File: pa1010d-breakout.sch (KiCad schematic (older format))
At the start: 2 parts, among them J1 Conn_01x08_Male, U1 PA1010D

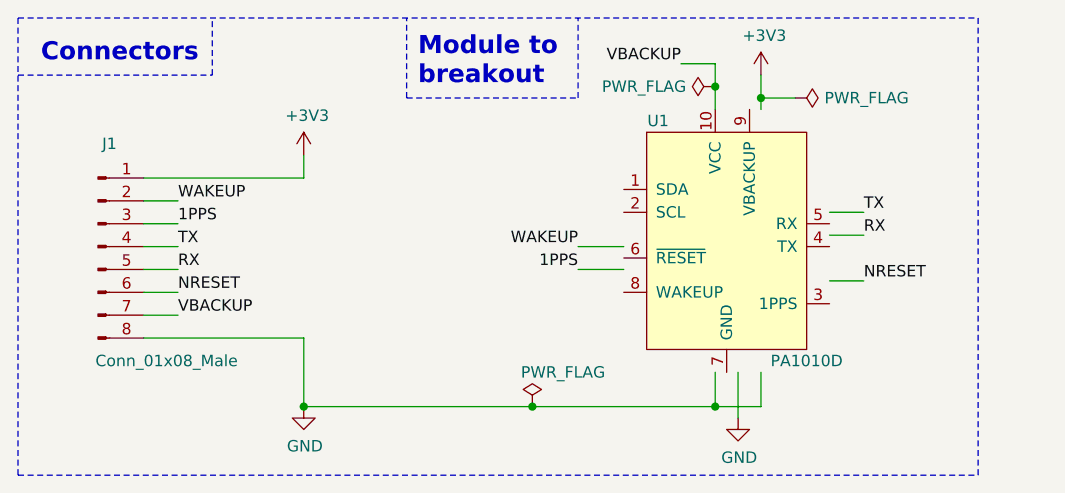
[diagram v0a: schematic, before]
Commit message: refactor: update schematic according to datasheet V0.3
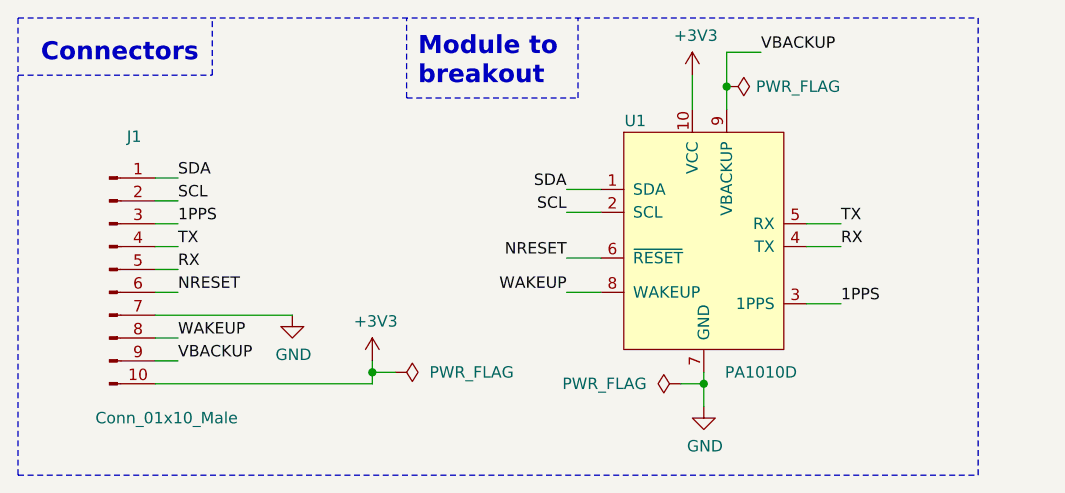
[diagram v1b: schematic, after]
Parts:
- removed J1: Conn_01x08_Male, Connector_PinHeader_2.54mm:PinHeader_1x08_P2.54mm_Vertical, symbol Connector:Conn_01x08_Male
- added J1: Conn_01x10_Male, symbol Connector:Conn_01x10_Male
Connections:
- net labels added: SCL, SDA
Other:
- moved on the sheet: U1
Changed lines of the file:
@@
 EESchema Schematic File Version 4
-LIBS:pa1010d-breakout-cache
-EELAYER 29 0
+EELAYER 30 0
 EELAYER END
 $Descr A4 11693 8268
@@
 Comment4 ""
 $EndDescr
-$Comp
-L CDTop_PA1010D:PA1010D U1
-U 1 1 5DD3ABC6
-P 6900 3600
-F 0 "U1" H 6600 4100 50  0000 C CNN
-F 1 "PA1010D" H 7250 3050 50  0000 C CNN
-F 2 "CDTop_PA1010D:CDTop_MT3333_PA1010D" H 6950 3500 50  0001 C CNN
-F 3 "" H 6950 3500 50  0001 C CNN
-	1    6900 3600
-	1    0    0    -1
-$EndComp
-Text Label 4500 3450 0    50   ~ 0
+Text Label 4500 4050 0    50   ~ 0
 WAKEUP
 Text Label 4500 3550 0    50   ~ 0
@@
 Text Label 4500 3850 0    50   ~ 0
 NRESET
-Text Label 4500 3950 0    50   ~ 0
+Text Label 4500 4150 0    50   ~ 0
 VBACKUP
-Wire Wire Line
-	4350 3450 4500 3450
-Wire Wire Line
-	4350 3550 4500 3550
-Wire Wire Line
-	4350 3650 4500 3650
-Wire Wire Line
-	4350 3750 4500 3750
-$Comp
-L power:GND #PWR0101
-U 1 1 5DD472DC
-P 5050 4350
-F 0 "#PWR0101" H 5050 4100 50  0001 C CNN
-F 1 "GND" H 5055 4177 50  0000 C CNN
-F 2 "" H 5050 4350 50  0001 C CNN
-F 3 "" H 5050 4350 50  0001 C CNN
-	1    5050 4350
-	1    0    0    -1
-$EndComp
-Wire Wire Line
-	6850 4200 6850 4350
-Wire Wire Line
-	6850 4350 7050 4350
-Wire Wire Line
-	7050 4350 7050 4200
 $Comp
 L power:GND #PWR0102
 U 1 1 5DD482B9
-P 6950 4400
-F 0 "#PWR0102" H 6950 4150 50  0001 C CNN
-F 1 "GND" H 6955 4227 50  0000 C CNN
-F 2 "" H 6950 4400 50  0001 C CNN
-F 3 "" H 6950 4400 50  0001 C CNN
-	1    6950 4400
-	1    0    0    -1
-$EndComp
-$Comp
-L power:+3V3 #PWR0103
-U 1 1 5DD48B19
-P 7050 2900
-F 0 "#PWR0103" H 7050 2750 50  0001 C CNN
-F 1 "+3V3" H 7065 3073 50  0000 C CNN
-F 2 "" H 7050 2900 50  0001 C CNN
-F 3 "" H 7050 2900 50  0001 C CNN
-	1    7050 2900
+P 6800 4350
+F 0 "#PWR0102" H 6800 4100 50  0001 C CNN
+F 1 "GND" H 6805 4177 50  0000 C CNN
+F 2 "" H 6800 4350 50  0001 C CNN
+F 3 "" H 6800 4350 50  0001 C CNN
+	1    6800 4350
 	1    0    0    -1
 $EndComp
@@
 L power:+3V3 #PWR0104
 U 1 1 5DD48B70
-P 5050 3250
-F 0 "#PWR0104" H 5050 3100 50  0001 C CNN
-F 1 "+3V3" H 5065 3423 50  0000 C CNN
-F 2 "" H 5050 3250 50  0001 C CNN
-F 3 "" H 5050 3250 50  0001 C CNN
-	1    5050 3250
-	1    0    0    -1
-$EndComp
-Wire Wire Line
-	7050 3050 7050 3000
-Text Label 6250 3650 2    50   ~ 0
+P 5350 4150
+F 0 "#PWR0104" H 5350 4000 50  0001 C CNN
+F 1 "+3V3" H 5365 4323 50  0000 C CNN
+F 2 "" H 5350 4150 50  0001 C CNN
+F 3 "" H 5350 4150 50  0001 C CNN
+	1    5350 4150
+	1    0    0    -1
+$EndComp
+Text Label 6200 3850 2    50   ~ 0
 WAKEUP
-Text Label 6250 3750 2    50   ~ 0
+Text Label 7400 3900 0    50   ~ 0
 1PPS
-Wire Wire Line
-	6250 3650 6450 3650
-Wire Wire Line
-	6250 3750 6450 3750
-Text Label 7500 3500 0    50   ~ 0
+Text Label 7400 3550 0    50   ~ 0
 TX
-Text Label 7500 3600 0    50   ~ 0
+Text Label 7400 3650 0    50   ~ 0
 RX
-Text Label 7500 3800 0    50   ~ 0
+Text Label 6200 3700 2    50   ~ 0
 NRESET
-Wire Wire Line
-	7350 3500 7500 3500
-Wire Wire Line
-	7350 3600 7500 3600
-Wire Wire Line
-	7350 3800 7500 3800
-Text Label 6700 2850 2    50   ~ 0
+Text Label 7050 2800 0    50   ~ 0
 VBACKUP
-Wire Wire Line
-	6700 2850 6850 2850
-Wire Wire Line
-	6850 2850 6850 2950
 $Comp
 L power:PWR_FLAG #FLG0102
 U 1 1 5DD4CF24
-P 7200 3000
-F 0 "#FLG0102" H 7200 3075 50  0001 C CNN
-F 1 "PWR_FLAG" V 7200 3128 50  0000 L CNN
-F 2 "" H 7200 3000 50  0001 C CNN
-F 3 "~" H 7200 3000 50  0001 C CNN
-	1    7200 3000
+P 6900 2950
+F 0 "#FLG0102" H 6900 3025 50  0001 C CNN
+F 1 "PWR_FLAG" V 6900 3078 50  0000 L CNN
+F 2 "" H 6900 2950 50  0001 C CNN
+F 3 "~" H 6900 2950 50  0001 C CNN
+	1    6900 2950
 	0    1    1    0
 $EndComp
-Wire Wire Line
-	7200 3000 7050 3000
-Connection ~ 7050 3000
-Wire Wire Line
-	7050 3000 7050 2900
-$Comp
-L power:PWR_FLAG #FLG0104
-U 1 1 5DD4EDC1
-P 6850 2950
-F 0 "#FLG0104" H 6850 3025 50  0001 C CNN
-F 1 "PWR_FLAG" V 6850 3077 50  0000 L CNN
-F 2 "" H 6850 2950 50  0001 C CNN
-F 3 "~" H 6850 2950 50  0001 C CNN
-	1    6850 2950
-	0    -1   -1   0
-$EndComp
-Connection ~ 6850 2950
-Wire Wire Line
-	6850 2950 6850 3050
 Wire Notes Line
 	3800 4650 3800 2650
@@
 Wire Notes Line
 	6250 3000 6250 2650
-Wire Wire Line
-	6950 4200 6950 4400
-$Comp
-L Connector:Conn_01x08_Male J1
-U 1 1 5DD3EF9A
-P 4150 3650
-F 0 "J1" H 4200 4100 50  0000 C CNN
-F 1 "Conn_01x08_Male" H 4450 3150 50  0000 C CNN
-F 2 "Connector_PinHeader_2.54mm:PinHeader_1x08_P2.54mm_Vertical" H 4150 3650 50  0001 C CNN
-F 3 "~" H 4150 3650 50  0001 C CNN
-	1    4150 3650
-	1    0    0    -1
-$EndComp
-Wire Wire Line
-	4350 3850 4500 3850
-Wire Wire Line
-	4350 3950 4500 3950
-Wire Wire Line
-	4350 3350 5050 3350
-Wire Wire Line
-	5050 3350 5050 3250
 $Comp
 L power:PWR_FLAG #FLG0101
 U 1 1 5DD47A81
-P 6050 4350
-F 0 "#FLG0101" H 6050 4425 50  0001 C CNN
-F 1 "PWR_FLAG" H 6000 4500 50  0000 L CNN
-F 2 "" H 6050 4350 50  0001 C CNN
-F 3 "~" H 6050 4350 50  0001 C CNN
-	1    6050 4350
-	1    0    0    -1
+P 6700 4250
+F 0 "#FLG0101" H 6700 4325 50  0001 C CNN
+F 1 "PWR_FLAG" V 6700 4400 50  0000 L CNN
+F 2 "" H 6700 4250 50  0001 C CNN
+F 3 "~" H 6700 4250 50  0001 C CNN
+	1    6700 4250
+	0    -1   -1   0
 $EndComp
 Wire Notes Line
@@
 Wire Notes Line
 	5500 3000 5500 2650
-Wire Wire Line
-	6850 4350 6050 4350
-Connection ~ 6850 4350
-Wire Wire Line
-	5050 4050 5050 4350
-Connection ~ 5050 4350
-Connection ~ 6050 4350
-Wire Wire Line
-	6050 4350 5050 4350
-Wire Wire Line
-	4350 4050 5050 4050
+$Comp
+L power:+3V3 #PWR0103
+U 1 1 5DD48B19
+P 6750 2900
+F 0 "#PWR0103" H 6750 2750 50  0001 C CNN
+F 1 "+3V3" H 6765 3073 50  0000 C CNN
+F 2 "" H 6750 2900 50  0001 C CNN
+F 3 "" H 6750 2900 50  0001 C CNN
+	1    6750 2900
+	1    0    0    -1
+$EndComp
+$Comp
+L CDTop_PA1010D:PA1010D U1
+U 1 1 5DD3ABC6
+P 6800 3600
+F 0 "U1" H 6500 4100 50  0000 C CNN
+F 1 "PA1010D" H 7050 3000 50  0000 C CNN
+F 2 "CDTop_PA1010D:CDTop_MT3333_PA1010D" H 6850 3500 50  0001 C CNN
+F 3 "https://drive.google.com/file/d/1O-9RGAwgs2fgtnzJRBa9eB1fAqJt7n_k/view" H 6850 3500 50  0001 C CNN
+	1    6800 3600
+	1    0    0    -1
+$EndComp
+Wire Wire Line
+	6800 4350 6800 4250
+Wire Wire Line
+	6350 3850 6200 3850
+Wire Wire Line
+	6350 3700 6200 3700
+Wire Wire Line
+	7250 3550 7400 3550
+Wire Wire Line
+	7250 3650 7400 3650
+Wire Wire Line
+	7250 3900 7400 3900
+Wire Wire Line
+	6750 2900 6750 3050
+Wire Wire Line
+	6900 3050 6900 2950
+Wire Wire Line
+	6900 2800 7050 2800
+Connection ~ 6900 2950
+Wire Wire Line
+	6900 2950 6900 2800
+$Comp
+L Connector:Conn_01x10_Male J1
+U 1 1 5DFB955C
+P 4200 3750
+F 0 "J1" H 4308 4331 50  0000 C CNN
+F 1 "Conn_01x10_Male" H 4450 3100 50  0000 C CNN
+F 2 "" H 4200 3750 50  0001 C CNN
+F 3 "~" H 4200 3750 50  0001 C CNN
+	1    4200 3750
+	1    0    0    -1
+$EndComp
+Text Label 6200 3500 2    50   ~ 0
+SCL
+Text Label 4500 3450 0    50   ~ 0
+SCL
+Wire Wire Line
+	6200 3500 6350 3500
+$Comp
+L power:GND #PWR01
+U 1 1 5DFC0BDB
+P 5000 3950
+F 0 "#PWR01" H 5000 3700 50  0001 C CNN
+F 1 "GND" H 5005 3777 50  0000 C CNN
+F 2 "" H 5000 3950 50  0001 C CNN
+F 3 "" H 5000 3950 50  0001 C CNN
+	1    5000 3950
+	1    0    0    -1
+$EndComp
+Wire Wire Line
+	4400 3450 4500 3450
+Wire Wire Line
+	4400 3550 4500 3550
+Wire Wire Line
+	4400 3650 4500 3650
+Wire Wire Line
+	4400 3750 4500 3750
+Wire Wire Line
+	4400 3850 4500 3850
+Wire Wire Line
+	4400 4050 4500 4050
+Wire Wire Line
+	4400 4150 4500 4150
+Wire Wire Line
+	4400 3950 5000 3950
+Wire Wire Line
+	4400 4250 5350 4250
+Wire Wire Line
+	6700 4250 6800 4250
+Connection ~ 6800 4250
+Wire Wire Line
+	6800 4250 6800 4200
+$Comp
+L power:PWR_FLAG #FLG0103
+U 1 1 5DFC64D0
+P 5450 4200
+F 0 "#FLG0103" H 5450 4275 50  0001 C CNN
+F 1 "PWR_FLAG" V 5450 4350 50  0000 L CNN
+F 2 "" H 5450 4200 50  0001 C CNN
+F 3 "~" H 5450 4200 50  0001 C CNN
+	1    5450 4200
+	0    1    1    0
+$EndComp
+Wire Wire Line
+	5350 4150 5350 4200
+Wire Wire Line
+	5450 4200 5350 4200
+Connection ~ 5350 4200
+Wire Wire Line
+	5350 4200 5350 4250
+Text Label 6200 3400 2    50   ~ 0
+SDA
+Wire Wire Line
+	6200 3400 6350 3400
+Text Label 4500 3350 0    50   ~ 0
+SDA
+Wire Wire Line
+	4400 3350 4500 3350
 $EndSCHEMATC

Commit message: refactor: elongate, rotate pads for PA1010D datasheet V0.3
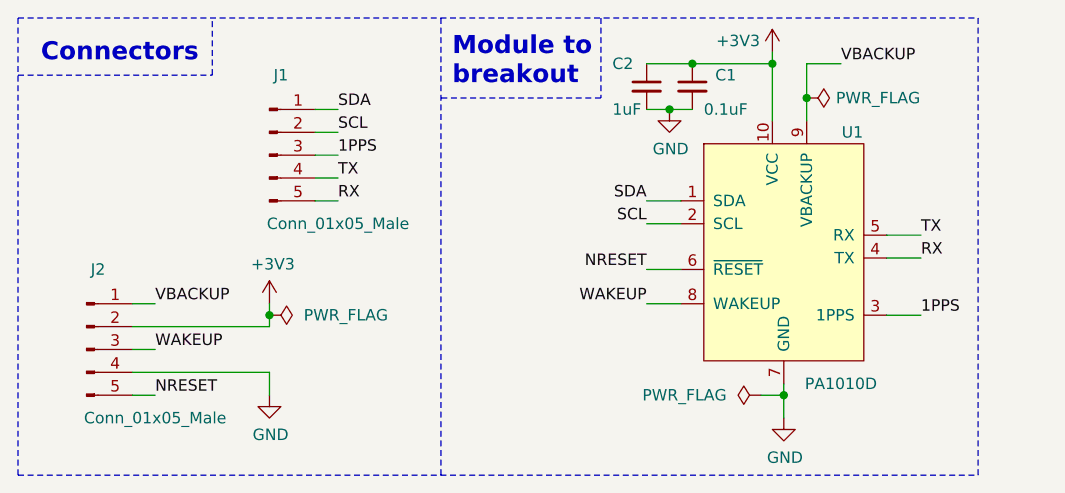
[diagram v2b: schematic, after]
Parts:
- removed J1: Conn_01x10_Male, symbol Connector:Conn_01x10_Male
- added C1: 0.1uF, Passives:C_0805_2012Metric_Pad1.15x1.40mm_HandSolder, symbol Device:C_Small
- added C2: 1uF, Passives:C_0805_2012Metric_Pad1.15x1.40mm_HandSolder, symbol Device:C_Small
- added J1, J2: Conn_01x05_Male, Connector_PinHeader_2.54mm:PinHeader_1x05_P2.54mm_Vertical, symbol Connector:Conn_01x05_Male
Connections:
- net +3V3: now also C1.1, C2.1, J2.2 (Pin_2)
- net 1PPS: now also J1.3 (Pin_3)
- net GND: now also C1.2, C2.2, J2.4 (Pin_4)
- net NRESET: now also J2.5 (Pin_5)
- net RX: now also J1.5 (Pin_5)
- net SCL: now also J1.2 (Pin_2)
- net SDA: now also J1.1 (Pin_1)
- net TX: now also J1.4 (Pin_4)
- net VBACKUP: now also J2.1 (Pin_1)
- net WAKEUP: now also J2.3 (Pin_3)
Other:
- moved on the sheet: U1

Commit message: refactor: change pin layout for easier trace routing. close #4
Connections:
- net +3V3: now also J2.5 (Pin_5); no longer J2.2 (Pin_2)
- net GND: now also J2.2 (Pin_2); no longer J2.4 (Pin_4)
- net NRESET: now also J2.1 (Pin_1); no longer J2.5 (Pin_5)
- net RX: now also J1.2 (Pin_2); no longer J1.5 (Pin_5)
- net SCL: now also J1.4 (Pin_4); no longer J1.2 (Pin_2)
- net SDA: now also J1.5 (Pin_5); no longer J1.1 (Pin_1)
- net TX: now also J1.1 (Pin_1); no longer J1.4 (Pin_4)
- net VBACKUP: now also J2.4 (Pin_4); no longer J2.1 (Pin_1)
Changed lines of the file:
@@
 Text Label 5200 3250 0    50   ~ 0
 1PPS
-Text Label 5200 3350 0    50   ~ 0
+Text Label 5200 3050 0    50   ~ 0
 TX
-Text Label 5200 3450 0    50   ~ 0
+Text Label 5200 3150 0    50   ~ 0
 RX
-Text Label 4400 4300 0    50   ~ 0
+Text Label 4400 3900 0    50   ~ 0
 NRESET
-Text Label 4400 3900 0    50   ~ 0
+Text Label 4400 4200 0    50   ~ 0
 VBACKUP
 $Comp
@@
 L power:+3V3 #PWR0104
 U 1 1 5DD48B70
-P 4900 3900
-F 0 "#PWR0104" H 4900 3750 50  0001 C CNN
-F 1 "+3V3" H 4915 4073 50  0000 C CNN
-F 2 "" H 4900 3900 50  0001 C CNN
-F 3 "" H 4900 3900 50  0001 C CNN
-	1    4900 3900
+P 5200 4200
+F 0 "#PWR0104" H 5200 4050 50  0001 C CNN
+F 1 "+3V3" H 5215 4373 50  0000 C CNN
+F 2 "" H 5200 4200 50  0001 C CNN
+F 3 "" H 5200 4200 50  0001 C CNN
+	1    5200 4200
 	1    0    0    -1
 $EndComp
@@
 Text Label 6550 3550 2    50   ~ 0
 SCL
-Text Label 5200 3150 0    50   ~ 0
+Text Label 5200 3350 0    50   ~ 0
 SCL
 Wire Wire Line
@@
 L power:GND #PWR01
 U 1 1 5DFC0BDB
-P 4900 4300
-F 0 "#PWR01" H 4900 4050 50  0001 C CNN
-F 1 "GND" H 4905 4127 50  0000 C CNN
-F 2 "" H 4900 4300 50  0001 C CNN
-F 3 "" H 4900 4300 50  0001 C CNN
-	1    4900 4300
+P 4850 4000
+F 0 "#PWR01" H 4850 3750 50  0001 C CNN
+F 1 "GND" H 4855 3827 50  0000 C CNN
+F 2 "" H 4850 4000 50  0001 C CNN
+F 3 "" H 4850 4000 50  0001 C CNN
+	1    4850 4000
 	1    0    0    -1
 $EndComp
@@
 	5100 3350 5200 3350
 Wire Wire Line
-	4300 4300 4400 4300
-Wire Wire Line
 	4300 4100 4400 4100
-Wire Wire Line
-	4300 4200 4900 4200
 Wire Wire Line
 	7050 4300 7150 4300
@@
 L power:PWR_FLAG #FLG0103
 U 1 1 5DFC64D0
-P 4900 3950
-F 0 "#FLG0103" H 4900 4025 50  0001 C CNN
-F 1 "PWR_FLAG" V 4900 4100 50  0000 L CNN
-F 2 "" H 4900 3950 50  0001 C CNN
-F 3 "~" H 4900 3950 50  0001 C CNN
-	1    4900 3950
+P 5200 4250
+F 0 "#FLG0103" H 5200 4325 50  0001 C CNN
+F 1 "PWR_FLAG" V 5300 4200 50  0000 L CNN
+F 2 "" H 5200 4250 50  0001 C CNN
+F 3 "~" H 5200 4250 50  0001 C CNN
+	1    5200 4250
 	0    1    1    0
 $EndComp
@@
 Wire Wire Line
 	6550 3450 6700 3450
-Text Label 5200 3050 0    50   ~ 0
+Text Label 5200 3450 0    50   ~ 0
 SDA
 Wire Wire Line
 	5100 3050 5200 3050
 Wire Wire Line
-	4900 3900 4900 3950
-Connection ~ 4900 3950
-Wire Wire Line
-	4900 3950 4900 4000
+	5200 4200 5200 4250
+Connection ~ 5200 4250
+Wire Wire Line
+	5200 4250 5200 4300
 Wire Notes Line
 	5650 2650 5650 4650
@@
 	1    0    0    -1
 $EndComp
-Wire Wire Line
-	4300 3900 4400 3900
-Wire Wire Line
-	4900 4200 4900 4300
 $Comp
 L Device:C_Small C1
@@
 	6350 3000 5650 3000
 Wire Wire Line
-	4300 4000 4900 4000
+	4300 4200 4400 4200
+Wire Wire Line
+	4300 4000 4850 4000
+Wire Wire Line
+	4300 4300 5200 4300
+Wire Wire Line
+	4300 3900 4400 3900
 $EndSCHEMATC

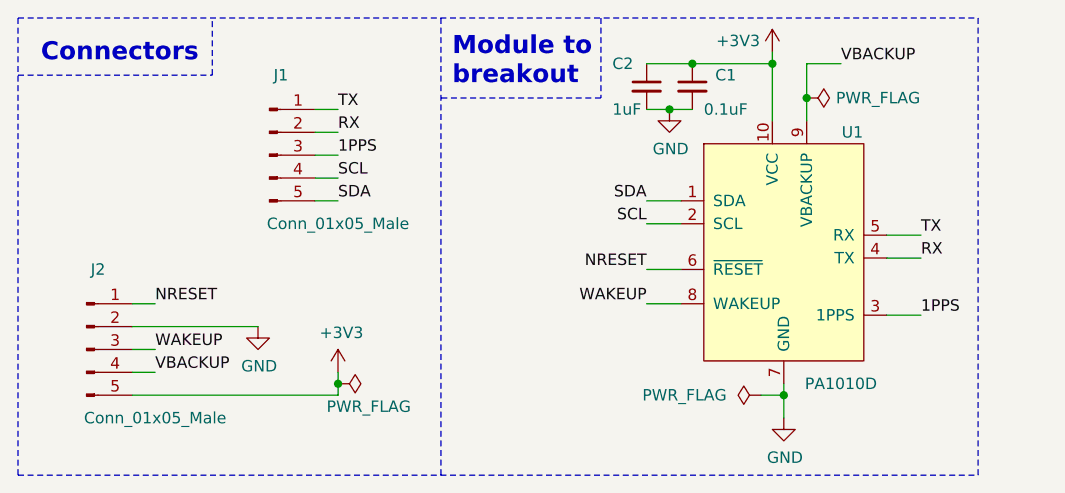
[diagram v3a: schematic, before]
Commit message: refactor: add pull up / down resistors
Co-authored-by: Chinmay Pendharkar <notthetup@gmail.com>
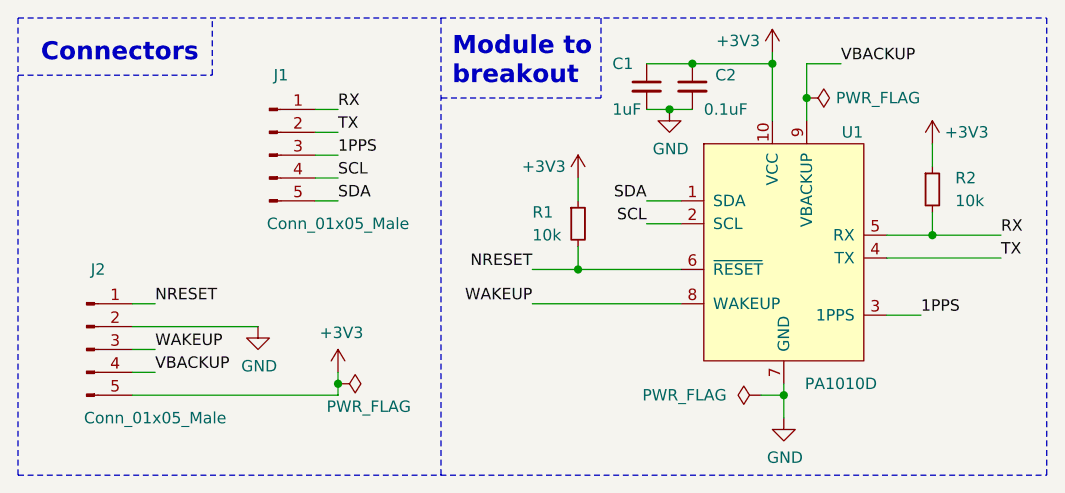
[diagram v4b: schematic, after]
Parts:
- added R1, R2: 10k, Passives:R_0805_2012Metric_Pad1.15x1.40mm_HandSolder, symbol Device:R_Small
- renumbered C2 to C1, C1 to C2
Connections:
- net +3V3: now also R1.1, R2.1
- net NRESET: now also R1.2
- net RX: now also J1.1 (Pin_1), U1.5 (RX), R2.2; no longer J1.2 (Pin_2), U1.4 (TX)
- net TX: now also J1.2 (Pin_2), U1.4 (TX); no longer J1.1 (Pin_1), U1.5 (RX)
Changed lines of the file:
@@
 Text Label 5200 3250 0    50   ~ 0
 1PPS
+Text Label 5200 3150 0    50   ~ 0
+TX
 Text Label 5200 3050 0    50   ~ 0
-TX
-Text Label 5200 3150 0    50   ~ 0
 RX
 Text Label 4400 3900 0    50   ~ 0
@@
 Text Label 4400 4200 0    50   ~ 0
 VBACKUP
-$Comp
-L power:GND #PWR0102
-U 1 1 5DD482B9
-P 7150 4400
-F 0 "#PWR0102" H 7150 4150 50  0001 C CNN
-F 1 "GND" H 7155 4227 50  0000 C CNN
-F 2 "" H 7150 4400 50  0001 C CNN
-F 3 "" H 7150 4400 50  0001 C CNN
-	1    7150 4400
-	1    0    0    -1
-$EndComp
 $Comp
 L power:+3V3 #PWR0104
@@
 	1    0    0    -1
 $EndComp
-Text Label 6550 3900 2    50   ~ 0
+Text Label 6050 3900 2    50   ~ 0
 WAKEUP
 Text Label 7750 3950 0    50   ~ 0
 1PPS
-Text Label 7750 3600 0    50   ~ 0
+Text Label 8100 3600 0    50   ~ 0
+RX
+Text Label 8100 3700 0    50   ~ 0
 TX
-Text Label 7750 3700 0    50   ~ 0
-RX
-Text Label 6550 3750 2    50   ~ 0
+Text Label 6050 3750 2    50   ~ 0
 NRESET
 Text Label 7400 2850 0    50   ~ 0
@@
 	0    -1   -1   0
 $EndComp
-Wire Notes Line
-	8000 2650 8000 4650
-Wire Notes Line
-	3800 4650 8000 4650
-Wire Notes Line
-	3800 2650 8000 2650
 $Comp
 L power:+3V3 #PWR0103
@@
 	1    0    0    -1
 $EndComp
-Wire Wire Line
-	7150 4400 7150 4300
-Wire Wire Line
-	6700 3900 6550 3900
-Wire Wire Line
-	6700 3750 6550 3750
-Wire Wire Line
-	7600 3600 7750 3600
-Wire Wire Line
-	7600 3700 7750 3700
 Wire Wire Line
 	7600 3950 7750 3950
@@
 $EndComp
 $Comp
-L Device:C_Small C1
+L Device:C_Small C2
 U 1 1 5DFC3652
 P 6750 2950
-F 0 "C1" H 6850 3000 50  0000 L CNN
+F 0 "C2" H 6850 3000 50  0000 L CNN
 F 1 "0.1uF" H 6800 2850 50  0000 L CNN
 F 2 "Passives:C_0805_2012Metric_Pad1.15x1.40mm_HandSolder" H 6750 2950 50  0001 C CNN
 F 3 "~" H 6750 2950 50  0001 C CNN
 	1    6750 2950
-	1    0    0    -1
-$EndComp
-$Comp
-L Device:C_Small C2
-U 1 1 5DFC3A5D
-P 6550 2950
-F 0 "C2" H 6400 3050 50  0000 L CNN
-F 1 "1uF" H 6400 2850 50  0000 L CNN
-F 2 "Passives:C_0805_2012Metric_Pad1.15x1.40mm_HandSolder" H 6550 2950 50  0001 C CNN
-F 3 "~" H 6550 2950 50  0001 C CNN
-	1    6550 2950
 	1    0    0    -1
 $EndComp
@@
 Wire Wire Line
 	4300 3900 4400 3900
+$Comp
+L Device:C_Small C1
+U 1 1 5DFC3A5D
+P 6550 2950
+F 0 "C1" H 6400 3050 50  0000 L CNN
+F 1 "1uF" H 6400 2850 50  0000 L CNN
+F 2 "Passives:C_0805_2012Metric_Pad1.15x1.40mm_HandSolder" H 6550 2950 50  0001 C CNN
+F 3 "~" H 6550 2950 50  0001 C CNN
+	1    6550 2950
+	1    0    0    -1
+$EndComp
+$Comp
+L Device:R_Small R2
+U 1 1 5E031692
+P 7800 3400
+F 0 "R2" H 7900 3450 50  0000 L CNN
+F 1 "10k" H 7900 3350 50  0000 L CNN
+F 2 "Passives:R_0805_2012Metric_Pad1.15x1.40mm_HandSolder" H 7800 3400 50  0001 C CNN
+F 3 "~" H 7800 3400 50  0001 C CNN
+	1    7800 3400
+	1    0    0    -1
+$EndComp
+$Comp
+L power:+3V3 #PWR03
+U 1 1 5E031B5A
+P 7800 3200
+F 0 "#PWR03" H 7800 3050 50  0001 C CNN
+F 1 "+3V3" H 7950 3250 50  0000 C CNN
+F 2 "" H 7800 3200 50  0001 C CNN
+F 3 "" H 7800 3200 50  0001 C CNN
+	1    7800 3200
+	1    0    0    -1
+$EndComp
+Wire Wire Line
+	7800 3200 7800 3300
+$Comp
+L power:GND #PWR0101
+U 1 1 5E03376C
+P 7150 4400
+F 0 "#PWR0101" H 7150 4150 50  0001 C CNN
+F 1 "GND" H 7155 4227 50  0000 C CNN
+F 2 "" H 7150 4400 50  0001 C CNN
+F 3 "" H 7150 4400 50  0001 C CNN
+	1    7150 4400
+	1    0    0    -1
+$EndComp
+Wire Wire Line
+	7150 4300 7150 4400
+Wire Wire Line
+	6050 3900 6700 3900
+Wire Wire Line
+	6050 3750 6250 3750
+Wire Wire Line
+	7600 3700 8100 3700
+$Comp
+L Device:R_Small R1
+U 1 1 5E03A4C9
+P 6250 3550
+F 0 "R1" H 6050 3600 50  0000 L CNN
+F 1 "10k" H 6050 3500 50  0000 L CNN
+F 2 "Passives:R_0805_2012Metric_Pad1.15x1.40mm_HandSolder" H 6250 3550 50  0001 C CNN
+F 3 "~" H 6250 3550 50  0001 C CNN
+	1    6250 3550
+	1    0    0    -1
+$EndComp
+$Comp
+L power:+3V3 #PWR04
+U 1 1 5E03A4CF
+P 6250 3350
+F 0 "#PWR04" H 6250 3200 50  0001 C CNN
+F 1 "+3V3" H 6100 3400 50  0000 C CNN
+F 2 "" H 6250 3350 50  0001 C CNN
+F 3 "" H 6250 3350 50  0001 C CNN
+	1    6250 3350
+	1    0    0    -1
+$EndComp
+Wire Wire Line
+	6250 3350 6250 3450
+Wire Wire Line
+	6250 3650 6250 3750
+Wire Wire Line
+	7600 3600 7800 3600
+Wire Wire Line
+	7800 3500 7800 3600
+Connection ~ 7800 3600
+Wire Wire Line
+	7800 3600 8100 3600
+Connection ~ 6250 3750
+Wire Wire Line
+	6250 3750 6700 3750
+Wire Notes Line
+	8300 2650 8300 4650
+Wire Notes Line
+	3800 4650 8300 4650
+Wire Notes Line
+	3800 2650 8300 2650
 $EndSCHEMATC
